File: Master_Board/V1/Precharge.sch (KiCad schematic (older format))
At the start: 16 parts

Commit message: Add Master_Board modules
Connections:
- wire segments 37 -> 38
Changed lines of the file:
@@
 $Descr A4 11693 8268
 encoding utf-8
-Sheet 8 10
+Sheet 7 10
 Title ""
 Date ""
@@
 L LTV-816S U?
 U 1 1 59454BA7
-P 4350 5600
-F 0 "U?" H 4350 5900 60  0000 C CNN
-F 1 "LTV-816S" H 4350 5400 60  0000 C CNN
-F 2 "IC:4-SMD" H 4350 4700 60  0001 C CNN
-F 3 "https://media.digikey.com/pdf/Data%20Sheets/Lite-On%20PDFs/LTV-816_826_846.pdf" H 4350 4600 60  0001 C CNN
-F 4 "Digikey" H 4350 5200 60  0001 C CNN "Supplier"
-F 5 "160-1361-5-ND" H 4350 5100 60  0001 C CNN "Supplier Part Number"
-F 6 "Lite-On Inc." H 4350 5000 60  0001 C CNN "Manufacturer"
-F 7 "LTV-816S" H 4350 4900 60  0001 C CNN "Manufacturer Part Number"
-F 8 "OPTOISOLATR 5KV TRANSISTOR 4-SMD" H 4350 4800 60  0001 C CNN "Description"
-	1    4350 5600
+P 4300 5600
+F 0 "U?" H 4300 5900 60  0000 C CNN
+F 1 "LTV-816S" H 4300 5400 60  0000 C CNN
+F 2 "IC:4-SMD" H 4300 4700 60  0001 C CNN
+F 3 "https://media.digikey.com/pdf/Data%20Sheets/Lite-On%20PDFs/LTV-816_826_846.pdf" H 4300 4600 60  0001 C CNN
+F 4 "Digikey" H 4300 5200 60  0001 C CNN "Supplier"
+F 5 "160-1361-5-ND" H 4300 5100 60  0001 C CNN "Supplier Part Number"
+F 6 "Lite-On Inc." H 4300 5000 60  0001 C CNN "Manufacturer"
+F 7 "LTV-816S" H 4300 4900 60  0001 C CNN "Manufacturer Part Number"
+F 8 "OPTOISOLATR 5KV TRANSISTOR 4-SMD" H 4300 4800 60  0001 C CNN "Description"
+	1    4300 5600
 	1    0    0    -1
 $EndComp
@@
 L DGND #PWR?
 U 1 1 59455900
-P 3950 5900
-F 0 "#PWR?" H 3950 5730 50  0001 C CNN
-F 1 "DGND" H 3950 5800 50  0000 C CNN
-F 2 "" H 3950 6000 60  0000 C CNN
-F 3 "" H 3930 5810 60  0000 C CNN
-	1    3950 5900
+P 3900 5900
+F 0 "#PWR?" H 3900 5730 50  0001 C CNN
+F 1 "DGND" H 3900 5800 50  0000 C CNN
+F 2 "" H 3900 6000 60  0000 C CNN
+F 3 "" H 3880 5810 60  0000 C CNN
+	1    3900 5900
 	1    0    0    -1
 $EndComp
@@
 	3900 3100 4100 3100
 Wire Wire Line
-	3950 5800 3950 5700
-Wire Wire Line
-	3950 5700 4150 5700
-Wire Wire Line
-	4150 5400 3650 5400
+	3900 5800 3900 5700
+Wire Wire Line
+	3900 5700 4100 5700
+Wire Wire Line
+	4100 5400 3650 5400
 Wire Wire Line
 	4100 2800 3600 2800
@@
 L DGND #PWR?
 U 1 1 59456C6B
-P 4800 5800
-F 0 "#PWR?" H 4800 5630 50  0001 C CNN
-F 1 "DGND" H 4800 5700 50  0000 C CNN
-F 2 "" H 4800 5900 60  0000 C CNN
-F 3 "" H 4780 5710 60  0000 C CNN
-	1    4800 5800
+P 4800 5900
+F 0 "#PWR?" H 4800 5730 50  0001 C CNN
+F 1 "DGND" H 4800 5800 50  0000 C CNN
+F 2 "" H 4800 6000 60  0000 C CNN
+F 3 "" H 4780 5810 60  0000 C CNN
+	1    4800 5900
 	1    0    0    -1
 $EndComp
@@
 $EndComp
 Wire Wire Line
-	4650 5700 4800 5700
-Wire Wire Line
-	4650 5400 6200 5400
+	4600 5400 6200 5400
 Wire Wire Line
 	5550 5100 5550 5400
@@
 Wire Wire Line
 	8200 5300 8300 5300
+Wire Wire Line
+	4800 5800 4800 5700
+Wire Wire Line
+	4800 5700 4600 5700
+Wire Notes Line
+	4300 4900 4300 3400
+Wire Notes Line
+	4300 2250 4300 950
+Wire Notes Line
+	4300 5950 4300 7100
 $EndSCHEMATC

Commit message: Add filter in VoltageSense
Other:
- note added: "Isolated"
- moved on the sheet: D?, F?, J?, R?, RL?

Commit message: Add page LedDriver
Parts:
- gave numbers to parts that had none: 16
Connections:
- net labels added: EX_PC_MAIN, EX_PC_MPPT
- wire segments 38 -> 48
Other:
- note added: "Precharge MPPT Contactor"
- note added: "Precharge Main Contactor"
- moved on the sheet: J701, J702
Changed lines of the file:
@@
 $Descr A4 11693 8268
 encoding utf-8
-Sheet 7 10
+Sheet 7 11
 Title ""
 Date ""
@@
 $EndDescr
 $Comp
-L LTV-816S U?
+L LTV-816S U701
 U 1 1 59454B00
 P 6300 2950
-F 0 "U?" H 6300 3250 60  0000 C CNN
+F 0 "U701" H 6300 3250 60  0000 C CNN
 F 1 "LTV-816S" H 6300 2750 60  0000 C CNN
 F 2 "IC:4-SMD" H 6300 2050 60  0001 C CNN
@@
 $EndComp
 $Comp
-L LTV-816S U?
+L LTV-816S U702
 U 1 1 59454BA7
 P 6300 5550
-F 0 "U?" H 6300 5850 60  0000 C CNN
+F 0 "U702" H 6300 5850 60  0000 C CNN
 F 1 "LTV-816S" H 6300 5350 60  0000 C CNN
 F 2 "IC:4-SMD" H 6300 4650 60  0001 C CNN
@@
 $EndComp
 $Comp
-L DGND #PWR?
+L DGND #PWR705
 U 1 1 594558D5
 P 6700 3250
-F 0 "#PWR?" H 6700 3080 50  0001 C CNN
+F 0 "#PWR705" H 6700 3080 50  0001 C CNN
 F 1 "DGND" H 6700 3150 50  0000 C CNN
 F 2 "" H 6700 3350 60  0000 C CNN
@@
 $EndComp
 $Comp
-L DGND #PWR?
+L DGND #PWR706
 U 1 1 59455900
 P 6700 5850
-F 0 "#PWR?" H 6700 5680 50  0001 C CNN
+F 0 "#PWR706" H 6700 5680 50  0001 C CNN
 F 1 "DGND" H 6700 5750 50  0000 C CNN
 F 2 "" H 6700 5950 60  0000 C CNN
@@
 PC_MPPT
 $Comp
-L NSR0530HT1G D?
+L NSR0530HT1G D702
 U 1 1 59455D44
 P 5100 2250
-F 0 "D?" V 5150 2050 60  0000 C CNN
+F 0 "D702" V 5150 2050 60  0000 C CNN
 F 1 "NSR0530HT1G" V 5000 1800 60  0000 C CNN
 F 2 "Diodes:SOD-323" H 5080 1250 60  0001 C CNN
@@
 $EndComp
 $Comp
-L ALQ112 RL?
+L ALQ112 RL702
 U 1 1 59455F37
 P 4200 2800
-F 0 "RL?" H 4200 3100 60  0000 C CNN
+F 0 "RL702" H 4200 3100 60  0000 C CNN
 F 1 "ALQ112" H 4250 2700 60  0000 C CNN
 F 2 "F" H 4200 1900 60  0001 C CNN
@@
 $EndComp
 $Comp
-L DGND #PWR?
+L DGND #PWR704
 U 1 1 5945622C
 P 5850 3250
-F 0 "#PWR?" H 5850 3080 50  0001 C CNN
+F 0 "#PWR704" H 5850 3080 50  0001 C CNN
 F 1 "DGND" H 5850 3150 50  0000 C CNN
 F 2 "" H 5850 3350 60  0000 C CNN
@@
 $EndComp
 $Comp
-L RC0805JR-071KL R?
+L RC0805JR-071KL R704
 U 1 1 594564D3
 P 5750 2000
-F 0 "R?" V 5700 2100 60  0000 C CNN
+F 0 "R704" V 5700 2100 60  0000 C CNN
 F 1 "RC0805JR-071KL" H 5750 1700 50  0001 C CNN
 F 2 "Resistors:R0805" H 5750 1100 30  0001 C CNN
@@
 $EndComp
 $Comp
-L 150080VS75000 D?
+L 150080VS75000 D704
 U 1 1 59456548
 P 5750 2450
-F 0 "D?" V 5550 2250 60  0000 C CNN
+F 0 "D704" V 5550 2250 60  0000 C CNN
 F 1 "150080VS75000" V 5650 1950 60  0000 C CNN
 F 2 "Diodes:LED_0805_GREEN" H 5760 1370 60  0001 C CNN
@@
 $EndComp
 $Comp
-L 12V #PWR?
+L 12V #PWR702
 U 1 1 5945671D
 P 5100 1550
-F 0 "#PWR?" H 5100 1400 50  0001 C CNN
+F 0 "#PWR702" H 5100 1400 50  0001 C CNN
 F 1 "12V" H 5090 1690 50  0000 C CNN
 F 2 "" H 5100 1550 60  0000 C CNN
@@
 	6500 2750 7000 2750
 Wire Wire Line
-	6000 3050 5850 3050
-Wire Wire Line
 	5850 3050 5850 3150
 Wire Wire Line
-	6000 2750 4450 2750
+	6000 2750 5750 2750
+Wire Wire Line
+	5750 2750 5100 2750
+Wire Wire Line
+	5100 2750 4450 2750
 Wire Wire Line
 	5100 2450 5100 2750
@@
 	4450 1750 4450 2600
 Wire Wire Line
-	5750 1750 4450 1750
-Wire Wire Line
-	5100 1550 5100 2150
+	4450 1750 5100 1750
+Wire Wire Line
+	5100 1750 5750 1750
+Wire Wire Line
+	5750 1750 7000 1750
+Wire Wire Line
+	5100 1550 5100 1750
+Wire Wire Line
+	5100 1750 5100 2150
 Connection ~ 5100 1750
 Wire Wire Line
@@
 Connection ~ 5750 2750
 $Comp
-L NSR0530HT1G D?
+L NSR0530HT1G D701
 U 1 1 59456C5A
 P 5050 4850
-F 0 "D?" V 5100 4650 60  0000 C CNN
+F 0 "D701" V 5100 4650 60  0000 C CNN
 F 1 "NSR0530HT1G" V 4950 4400 60  0000 C CNN
 F 2 "Diodes:SOD-323" H 5030 3850 60  0001 C CNN
@@
 $EndComp
 $Comp
-L ALQ112 RL?
+L ALQ112 RL701
 U 1 1 59456C65
 P 4150 5400
-F 0 "RL?" H 4150 5700 60  0000 C CNN
+F 0 "RL701" H 4150 5700 60  0000 C CNN
 F 1 "ALQ112" H 4200 5300 60  0000 C CNN
 F 2 "F" H 4150 4500 60  0001 C CNN
@@
 $EndComp
 $Comp
-L DGND #PWR?
+L DGND #PWR703
 U 1 1 59456C6B
 P 5800 5850
-F 0 "#PWR?" H 5800 5680 50  0001 C CNN
+F 0 "#PWR703" H 5800 5680 50  0001 C CNN
 F 1 "DGND" H 5800 5750 50  0000 C CNN
 F 2 "" H 5800 5950 60  0000 C CNN
@@
 $EndComp
 $Comp
-L RC0805JR-071KL R?
+L RC0805JR-071KL R703
 U 1 1 59456C79
 P 5700 4600
-F 0 "R?" V 5650 4700 60  0000 C CNN
+F 0 "R703" V 5650 4700 60  0000 C CNN
 F 1 "RC0805JR-071KL" H 5700 4300 50  0001 C CNN
 F 2 "Resistors:R0805" H 5700 3700 30  0001 C CNN
@@
 $EndComp
 $Comp
-L 12V #PWR?
+L 12V #PWR701
 U 1 1 59456C8C
 P 5050 4150
-F 0 "#PWR?" H 5050 4000 50  0001 C CNN
+F 0 "#PWR701" H 5050 4000 50  0001 C CNN
 F 1 "12V" H 5040 4290 50  0000 C CNN
 F 2 "" H 5050 4150 60  0000 C CNN
@@
 $EndComp
 Wire Wire Line
-	6000 5350 4400 5350
+	6000 5350 5700 5350
+Wire Wire Line
+	5700 5350 5050 5350
+Wire Wire Line
+	5050 5350 4400 5350
 Wire Wire Line
 	5050 5050 5050 5350
@@
 	4400 4350 4400 5200
 Wire Wire Line
-	5700 4350 4400 4350
-Wire Wire Line
-	5050 4150 5050 4750
+	4400 4350 5050 4350
+Wire Wire Line
+	5050 4350 5700 4350
+Wire Wire Line
+	5700 4350 7000 4350
+Wire Wire Line
+	5050 4150 5050 4350
+Wire Wire Line
+	5050 4350 5050 4750
 Connection ~ 5050 4350
 Wire Wire Line
 	5700 4400 5700 4350
 $Comp
-L 150080VS75000 D?
+L 150080VS75000 D703
 U 1 1 59456C86
 P 5700 5050
-F 0 "D?" V 5500 4850 60  0000 C CNN
+F 0 "D703" V 5500 4850 60  0000 C CNN
 F 1 "150080VS75000" V 5600 4550 60  0000 C CNN
 F 2 "Diodes:LED_0805_GREEN" H 5710 3970 60  0001 C CNN
@@
 	5700 4850 5700 4800
 $Comp
-L 39511000440 F?
+L 39511000440 F702
 U 1 1 5945789A
 P 3500 2600
-F 0 "F?" H 3500 2710 60  0000 C CNN
+F 0 "F702" H 3500 2710 60  0000 C CNN
 F 1 "39511000440" H 3500 2300 50  0001 C CNN
 F 2 "Fuses:TE5_395" H 3500 1700 30  0001 C CNN
@@
 $EndComp
 $Comp
-L 649002227222 J?
+L 649002227222 J701
 U 1 1 59457BA5
-P 2150 2750
-F 0 "J?" H 2150 2950 60  0000 C CNN
-F 1 "649002227222" H 2150 2600 60  0000 C CNN
-F 2 "Connectors:649002227222" H 2150 1850 60  0001 C CNN
-F 3 "http://katalog.we-online.de/em/datasheet/649016227222.pdf" H 2150 1750 60  0001 C CNN
-F 4 "Digikey" H 2150 2350 60  0001 C CNN "Supplier"
-F 5 "732-1937-ND" H 2150 2250 60  0001 C CNN "Supplier Part Number"
-F 6 "Wurth Electronics Inc." H 2150 2150 60  0001 C CNN "Manufacturer"
-F 7 "649002227222" H 2150 2050 60  0001 C CNN "Manufacturer Part Number"
-F 8 "HEADER MALE DUAL ANGLE W/MNT 2P" H 2150 1950 60  0001 C CNN "Description"
-	1    2150 2750
+P 1400 2750
+F 0 "J701" H 1400 2950 60  0000 C CNN
+F 1 "649002227222" H 1400 2600 60  0000 C CNN
+F 2 "Connectors:649002227222" H 1400 1850 60  0001 C CNN
+F 3 "http://katalog.we-online.de/em/datasheet/649016227222.pdf" H 1400 1750 60  0001 C CNN
+F 4 "Digikey" H 1400 2350 60  0001 C CNN "Supplier"
+F 5 "732-1937-ND" H 1400 2250 60  0001 C CNN "Supplier Part Number"
+F 6 "Wurth Electronics Inc." H 1400 2150 60  0001 C CNN "Manufacturer"
+F 7 "649002227222" H 1400 2050 60  0001 C CNN "Manufacturer Part Number"
+F 8 "HEADER MALE DUAL ANGLE W/MNT 2P" H 1400 1950 60  0001 C CNN "Description"
+	1    1400 2750
 	1    0    0    -1
 $EndComp
 Wire Wire Line
-	3950 2750 2350 2750
+	3950 2750 1600 2750
 Wire Wire Line
 	3950 2600 3700 2600
 $Comp
-L TR50JBC100R R?
+L TR50JBC100R R702
 U 1 1 59458C40
 P 2850 2600
-F 0 "R?" H 2850 2680 60  0000 C CNN
+F 0 "R702" H 2850 2680 60  0000 C CNN
 F 1 "TR50JBC100R" H 2850 2300 50  0001 C CNN
 F 2 "Resistors:TR50" H 2850 1700 30  0001 C CNN
@@
 	2450 2600 2450 2650
 Wire Wire Line
-	2450 2650 2350 2650
-$Comp
-L 39511000440 F?
+	2450 2650 1600 2650
+$Comp
+L 39511000440 F701
 U 1 1 59458F9F
 P 3450 5200
-F 0 "F?" H 3450 5310 60  0000 C CNN
+F 0 "F701" H 3450 5310 60  0000 C CNN
 F 1 "39511000440" H 3450 4900 50  0001 C CNN
 F 2 "Fuses:TE5_395" H 3450 4300 30  0001 C CNN
@@
 $EndComp
 $Comp
-L 649002227222 J?
+L 649002227222 J702
 U 1 1 59458FAA
-P 2100 5350
-F 0 "J?" H 2100 5550 60  0000 C CNN
-F 1 "649002227222" H 2100 5200 60  0000 C CNN
-F 2 "Connectors:649002227222" H 2100 4450 60  0001 C CNN
-F 3 "http://katalog.we-online.de/em/datasheet/649016227222.pdf" H 2100 4350 60  0001 C CNN
-F 4 "Digikey" H 2100 4950 60  0001 C CNN "Supplier"
-F 5 "732-1937-ND" H 2100 4850 60  0001 C CNN "Supplier Part Number"
-F 6 "Wurth Electronics Inc." H 2100 4750 60  0001 C CNN "Manufacturer"
-F 7 "649002227222" H 2100 4650 60  0001 C CNN "Manufacturer Part Number"
-F 8 "HEADER MALE DUAL ANGLE W/MNT 2P" H 2100 4550 60  0001 C CNN "Description"
-	1    2100 5350
+P 1400 5350
+F 0 "J702" H 1400 5550 60  0000 C CNN
+F 1 "649002227222" H 1400 5200 60  0000 C CNN
+F 2 "Connectors:649002227222" H 1400 4450 60  0001 C CNN
+F 3 "http://katalog.we-online.de/em/datasheet/649016227222.pdf" H 1400 4350 60  0001 C CNN
+F 4 "Digikey" H 1400 4950 60  0001 C CNN "Supplier"
+F 5 "732-1937-ND" H 1400 4850 60  0001 C CNN "Supplier Part Number"
+F 6 "Wurth Electronics Inc." H 1400 4750 60  0001 C CNN "Manufacturer"
+F 7 "649002227222" H 1400 4650 60  0001 C CNN "Manufacturer Part Number"
+F 8 "HEADER MALE DUAL ANGLE W/MNT 2P" H 1400 4550 60  0001 C CNN "Description"
+	1    1400 5350
 	1    0    0    -1
 $EndComp
 Wire Wire Line
-	3900 5350 2300 5350
+	3900 5350 1600 5350
 Wire Wire Line
 	3900 5200 3650 5200
 $Comp
-L TR50JBC100R R?
+L TR50JBC100R R701
 U 1 1 59458FBA
 P 2800 5200
-F 0 "R?" H 2800 5280 60  0000 C CNN
+F 0 "R701" H 2800 5280 60  0000 C CNN
 F 1 "TR50JBC100R" H 2800 4900 50  0001 C CNN
 F 2 "Resistors:TR50" H 2800 4300 30  0001 C CNN
@@
 	2400 5200 2400 5250
 Wire Wire Line
-	2400 5250 2300 5250
+	2400 5250 1600 5250
 Wire Wire Line
 	5800 5750 5800 5650
-Wire Wire Line
-	5800 5650 6000 5650
-Wire Notes Line
-	6300 4850 6300 3350
-Wire Notes Line
-	6300 2200 6300 900
-Wire Notes Line
-	6300 5900 6300 7050
 Text Notes 2100 1350 0    120  ~ 0
 Isolated
+Wire Notes Line
+	4200 2400 4200 1000
+Wire Notes Line
+	4200 3050 4200 5000
+Wire Notes Line
+	4200 5600 4200 7350
+Wire Notes Line
+	4200 7350 4150 7350
+Text HLabel 7000 1750 2    60   Output ~ 0
+EX_PC_MAIN
+Text HLabel 7000 4350 2    60   Output ~ 0
+EX_PC_MPPT
+Text Notes 1100 2250 0    120  ~ 0
+Precharge Main Contactor
+Text Notes 1100 4900 0    120  ~ 0
+Precharge MPPT Contactor
+Connection ~ 5750 1750
+Wire Wire Line
+	5850 3050 6000 3050
+Connection ~ 5700 4350
+Wire Wire Line
+	5800 5650 6000 5650
 $EndSCHEMATC

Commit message: Modify MasterBoard.sch
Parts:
- added D? (x2): C3D04060A, F, symbol C3D04060A
- added Q? (x2): BC849BLT1G, IC:SOT-23-3, symbol BC849BLT1G
- added R? (x2): RC0805JR-072K2L, Resistors:R0805, symbol RC0805JR-072K2L
- added R? (x2): RC0805JR-0710KL, Resistors:R0805, symbol RC0805JR-0710KL
- D703, D704: symbol 150080VS75000 -> 150080VS75000-RESCUE-Master_Board
- U701, U702: symbol LTV-816S -> LTV-816S-RESCUE-Master_Board
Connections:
- net labels added: 3.3V
- wire segments 48 -> 50
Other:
- moved on the sheet: D701, D702, D703, D704, F701, F702, J701, J702, R701, R702, R703, R704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

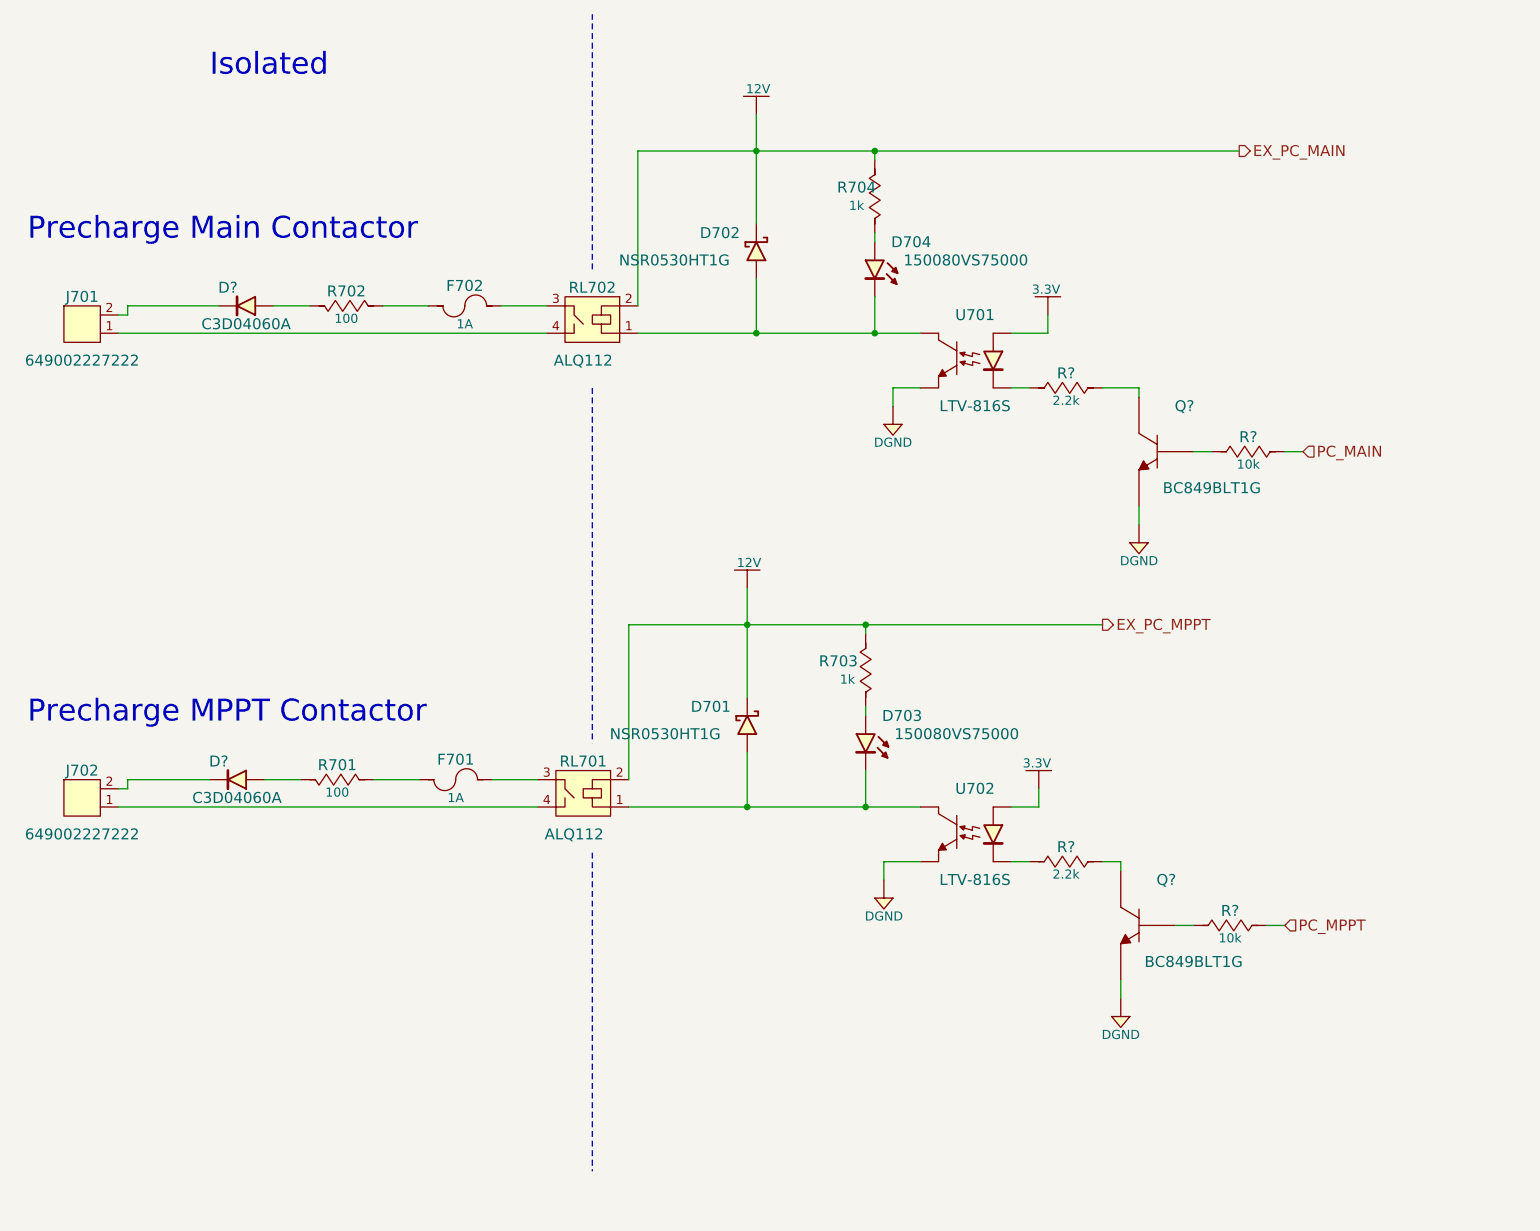
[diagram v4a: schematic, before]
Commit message: Add page LEDDriver.sch
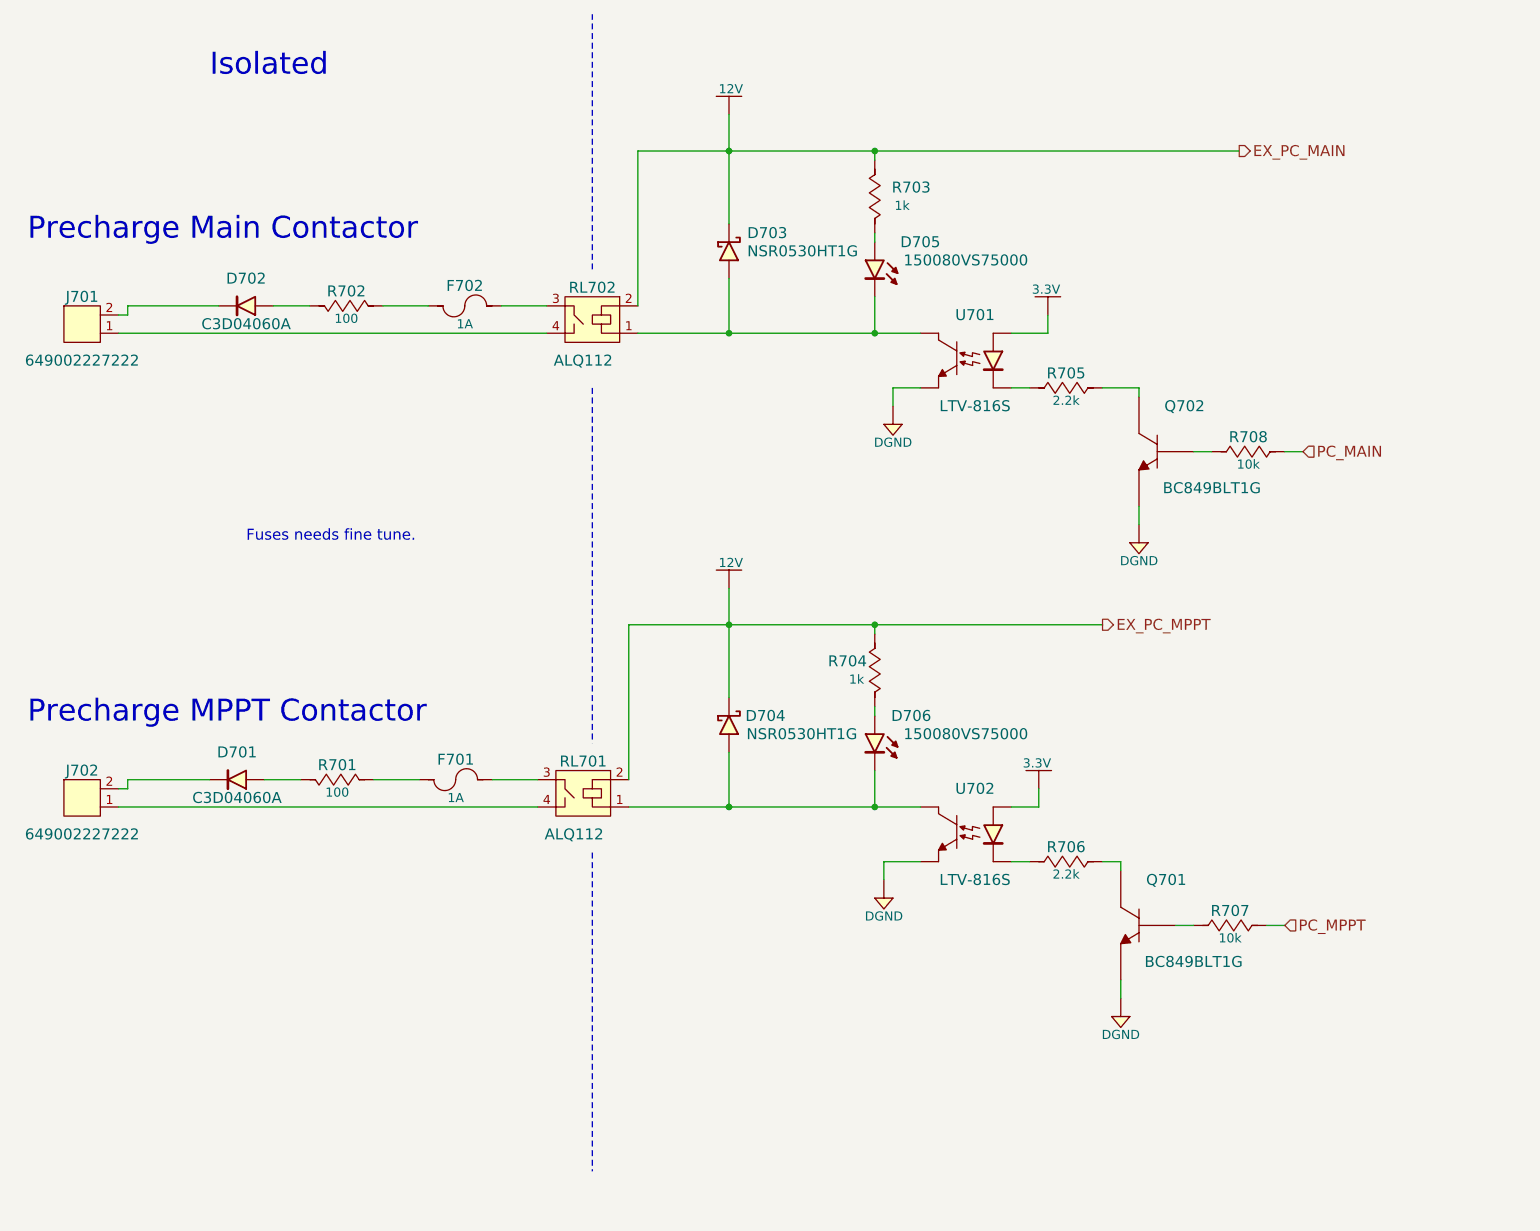
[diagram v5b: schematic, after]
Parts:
- removed D? (x2): C3D04060A, F, symbol C3D04060A
- added D701, D702: C3D04060A, Diodes:TO-220-2-D, symbol C3D04060A
- RL701, RL702: footprint F -> Relays:ALQ112
- gave numbers to parts that had none: 6
- renumbered D702 to D703, D701 to D704, D704 to D705, D703 to D706, R704 to R703, R703 to R704
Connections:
- net at J701.2: now also D702.1 (Cathode)
- net at R702.2: now also D702.2 (Anode)
- net at J702.2: now also D701.1 (Cathode)
- net at R701.2: now also D701.2 (Anode)
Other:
- note added: "Fuses needs fine tune."
- moved on the sheet: D703, D704, D706, R704
